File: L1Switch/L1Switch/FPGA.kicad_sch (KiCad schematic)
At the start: 3 parts, among them U1 XC7A15T-FTG256

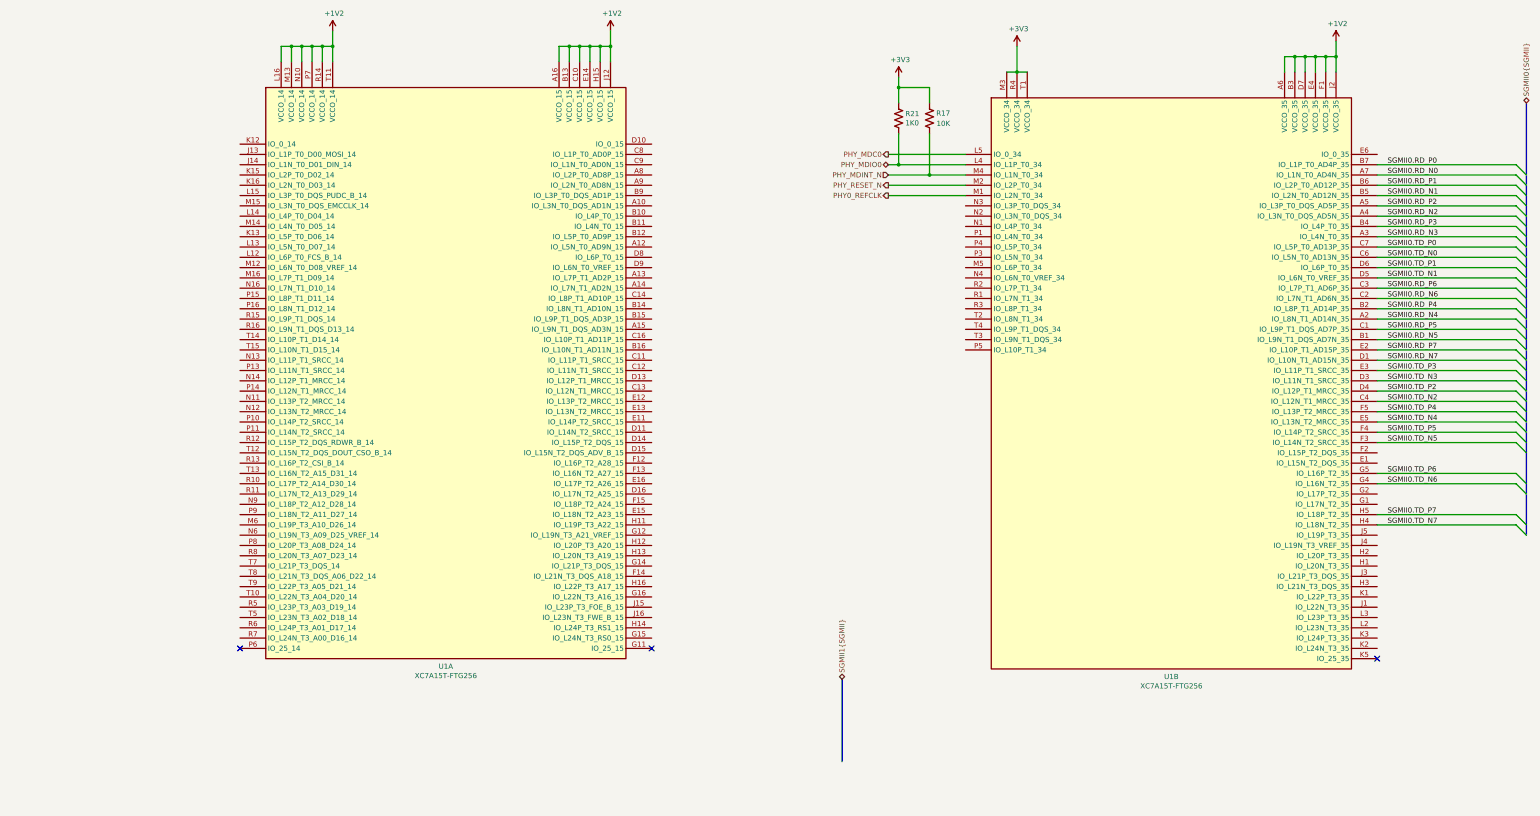
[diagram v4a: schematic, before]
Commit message: Add instance 3 and 4 of the network ports.
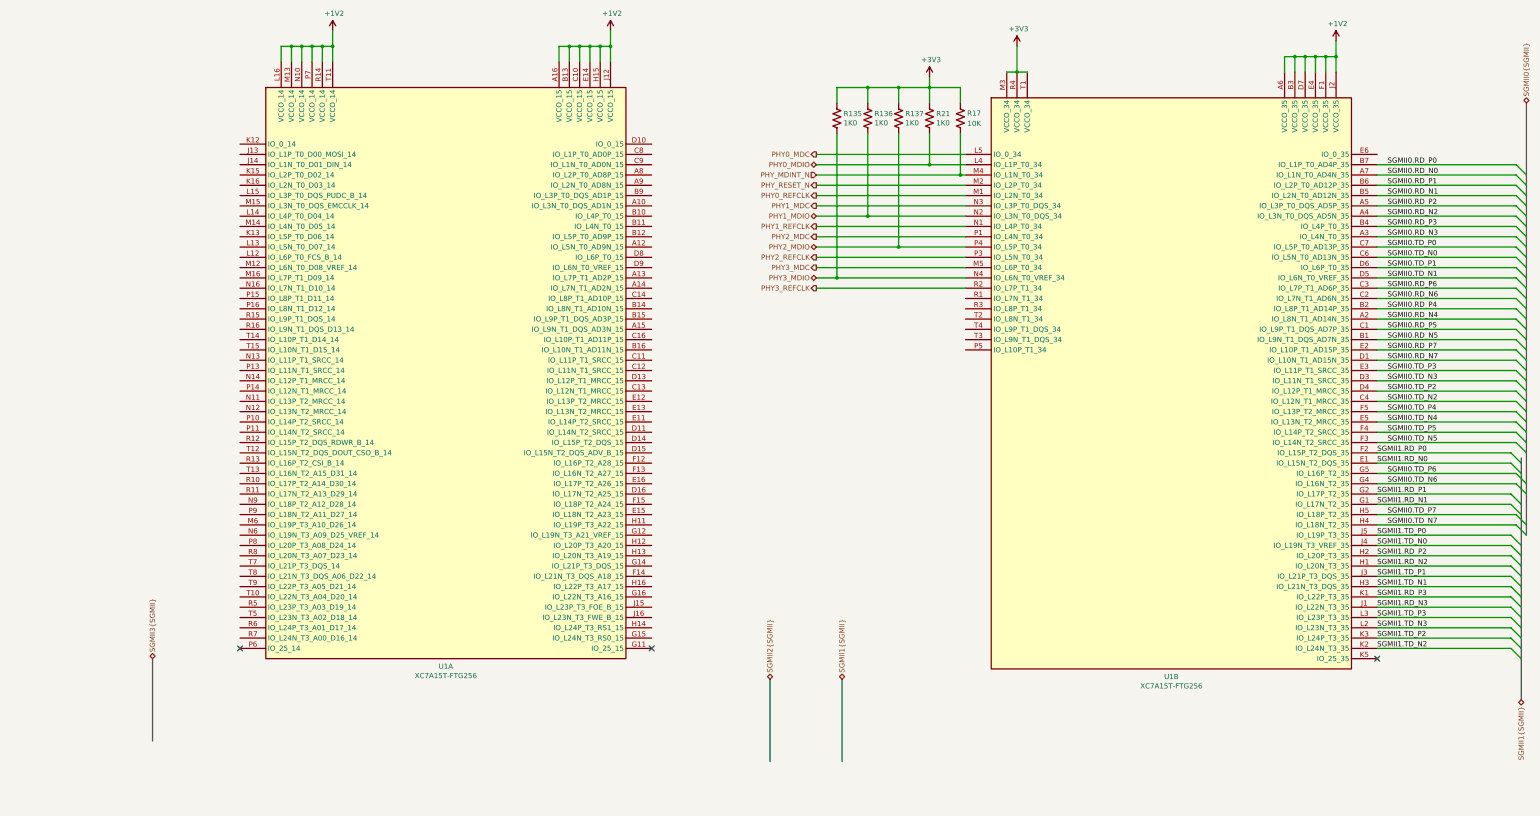
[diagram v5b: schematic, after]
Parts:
- added R135, R136, R137: 1K0, Resistor_SMD:R_0402_1005Metric, symbol Device:R_US
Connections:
- net +3V3: now also R135.1, R136.1, R137.1
- net SGMII1.RD_N0: now reaches U1.E1 (IO_L15N_T2_DQS_35)
- net SGMII1.RD_P0: now reaches U1.F2 (IO_L15P_T2_DQS_35)
- net SGMII1.RD_N1: now reaches U1.G1 (IO_L17N_T2_35)
- net SGMII1.RD_P1: now reaches U1.G2 (IO_L17P_T2_35)
- net SGMII1.RD_N2: now reaches U1.H1 (IO_L20N_T3_35)
- net SGMII1.RD_P2: now reaches U1.H2 (IO_L20P_T3_35)
- net SGMII1.TD_N1: now reaches U1.H3 (IO_L21N_T3_DQS_35)
- net SGMII1.RD_N3: now reaches U1.J1 (IO_L22N_T3_35)
- net SGMII1.TD_P1: now reaches U1.J3 (IO_L21P_T3_DQS_35)
- net SGMII1.TD_N0: now reaches U1.J4 (IO_L19N_T3_VREF_35)
- net SGMII1.TD_P0: now reaches U1.J5 (IO_L19P_T3_35)
- net SGMII1.RD_P3: now reaches U1.K1 (IO_L22P_T3_35)
- net SGMII1.TD_N2: now reaches U1.K2 (IO_L24N_T3_35)
- net SGMII1.TD_P2: now reaches U1.K3 (IO_L24P_T3_35)
- net SGMII1.TD_N3: now reaches U1.L2 (IO_L23N_T3_35)
- net SGMII1.TD_P3: now reaches U1.L3 (IO_L23P_T3_35)
- net PHY3_MDC: now reaches U1.M5 (IO_L6P_T0_34)
- net PHY1_REFCLK: now reaches U1.N1 (IO_L4P_T0_34)
- net PHY1_MDIO: now reaches U1.N2 (IO_L3N_T0_DQS_34)
- net PHY1_MDIO: now also R136.2
- net PHY1_MDC: now reaches U1.N3 (IO_L3P_T0_DQS_34)
- net PHY3_MDIO: now reaches U1.N4 (IO_L6N_T0_VREF_34)
- net PHY3_MDIO: now also R135.2
- net PHY2_MDC: now reaches U1.P1 (IO_L4N_T0_34)
- net PHY2_REFCLK: now reaches U1.P3 (IO_L5N_T0_34)
- net PHY2_MDIO: now reaches U1.P4 (IO_L5P_T0_34)
- net PHY2_MDIO: now also R137.2
- net PHY3_REFCLK: now reaches U1.R2 (IO_L7P_T1_34)
- net PHY_MDC0 renamed PHY0_MDC
- net PHY_MDIO0 renamed PHY0_MDIO
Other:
- moved on the sheet: R17, R21
